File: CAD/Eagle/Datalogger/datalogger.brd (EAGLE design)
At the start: 48.2 x 50.5 mm, 12 parts

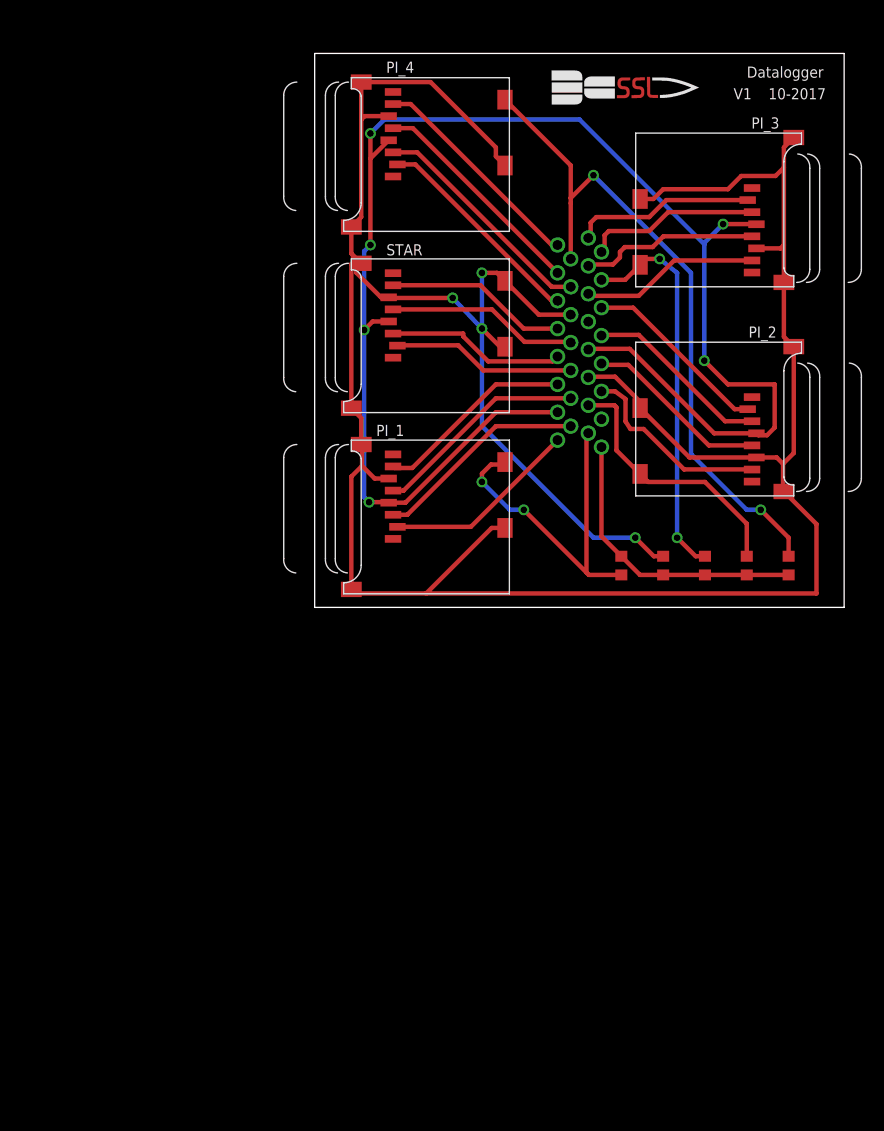
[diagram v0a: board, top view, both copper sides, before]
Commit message: Datalogger and STARduino
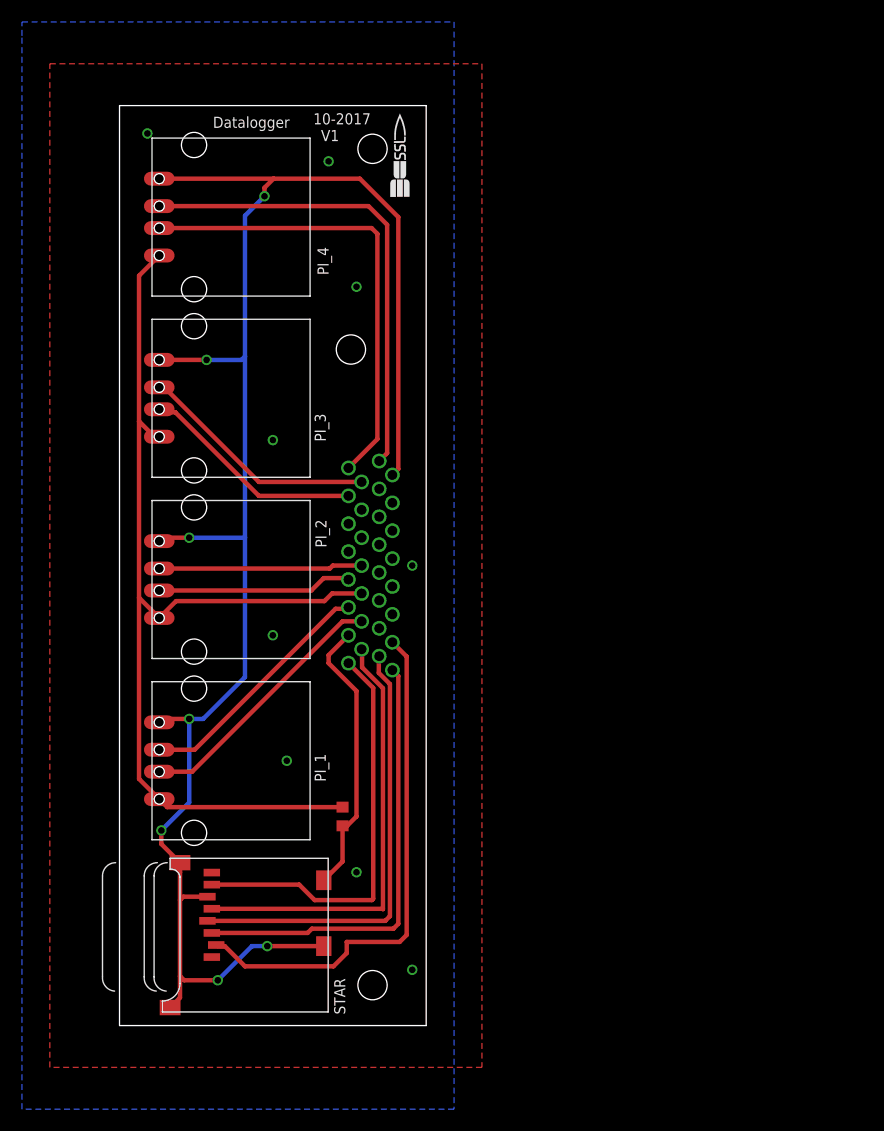
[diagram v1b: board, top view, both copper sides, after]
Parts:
- removed R1: 1M, resistor:R0603
- removed R2, R3, R4: (no value), resistor:R0603
- PI_1, PI_2, PI_3, PI_4: value MICROSD -> USB_A; device adafruit:MICROSD -> NR_connectors:USB_A
- U$1: value SSL.53IN -> SSL.3IN_SILK; device images:SSL_.53IN -> images:SSL_SILK_.3IN
- moved STAR 57.1 mm to (5.08, -22.9)
- moved PI_1 38.7 mm to (-3.81, -14.0)
- moved PI_3 38.2 mm to (-3.81, 19.1), turned to 270 degrees
- moved PI_2 37.6 mm to (-3.81, 2.54), turned to 270 degrees
- moved R5 37.1 mm to (6.35, -19.1), turned to 90 degrees
- moved PI_4 28.4 mm to (-3.81, 35.6)
- moved CONNECTOR 27.9 mm to (8.89, 3.81)
- moved U$1 19.3 mm to (10.4, 37.4), turned to 0 degrees
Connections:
- removed net CS_PI_1: CONNECTOR.17, PI_1.2
- removed net CS_PI_2: CONNECTOR.11, PI_2.2
- removed net CS_PI_3: CONNECTOR.16, PI_3.2
- removed net CS_PI_4: CONNECTOR.27, PI_4.2
- removed net MISO_PI_1: CONNECTOR.21, PI_1.7
- removed net MISO_PI_2: CONNECTOR.5, PI_2.7
- removed net MISO_PI_3: CONNECTOR.12, PI_3.7
- removed net MISO_PI_4: CONNECTOR.31, PI_4.7
- removed net MOSI_PI_1: CONNECTOR.18, PI_1.3
- removed net MOSI_PI_2: CONNECTOR.9, PI_2.3
- removed net MOSI_PI_3: CONNECTOR.15, PI_3.3
- removed net MOSI_PI_4: CONNECTOR.28, PI_4.3
- removed net SCK_PI_1: CONNECTOR.20, PI_1.5
- removed net SCK_PI_2: CONNECTOR.7, PI_2.5
- removed net SCK_PI_3: CONNECTOR.14, PI_3.5
- removed net SCK_PI_4: CONNECTOR.29, PI_4.5
- removed net SD_PI_1: CONNECTOR.2, PI_1.CD1, R1.1
- removed net SD_PI_2: CONNECTOR.4, PI_2.CD1, R2.1
- removed net SD_PI_3: CONNECTOR.13, PI_3.CD1, R3.1
- removed net SD_PI_4: CONNECTOR.30, PI_4.CD1, R4.1
- new net D: CONNECTOR.25
- new net DATA+1: CONNECTOR.21, PI_1.DATA+
- new net DATA+2: CONNECTOR.24, PI_2.DATA+
- new net DATA+3: CONNECTOR.30, PI_3.DATA+
- new net DATA+4: CONNECTOR.16, PI_4.DATA+
- new net DATA-1: CONNECTOR.20, PI_1.DATA-
- new net DATA-2: CONNECTOR.23, PI_2.DATA-
- new net DATA-3: CONNECTOR.29, PI_3.DATA-
- new net DATA-4: CONNECTOR.31, PI_4.DATA-
- new net FOUR: CONNECTOR.11
- new net N$7: CONNECTOR.12
- new net N$8: CONNECTOR.13
- new net ONE: CONNECTOR.27
- new net R: CONNECTOR.26
- new net THREE: CONNECTOR.10
- net +3V3: now also CONNECTOR.2; no longer CONNECTOR.19, CONNECTOR.8, PI_1.4, PI_2.4, PI_3.4, PI_4.4
- net +5V: now also CONNECTOR.22, PI_1.VCC, PI_2.VCC, PI_3.VCC, PI_4.VCC; no longer CONNECTOR.1, R1.2, R2.2, R3.2, R4.2
- net CS_STAR: now also CONNECTOR.3; no longer CONNECTOR.22
- net GND: now also CONNECTOR.15, PI_1.GND, PI_2.GND, PI_3.GND, PI_4.GND; no longer CONNECTOR.6, PI_1.6, PI_1.CD2, PI_1.MT1, PI_1.MT2, PI_2.6, PI_2.CD2, PI_2.MT1, PI_2.MT2, PI_3.6, PI_3.CD2, PI_3.MT1, PI_3.MT2, PI_4.6, PI_4.CD2, PI_4.MT1, PI_4.MT2
- net MISO_STAR: now also CONNECTOR.17; no longer CONNECTOR.25
- net MOSI_STAR: now also CONNECTOR.1; no longer CONNECTOR.23
- net SCK_STAR: now also CONNECTOR.18; no longer CONNECTOR.24
- net SD_STAR: now also CONNECTOR.19; no longer CONNECTOR.26
- net TWO: now also CONNECTOR.28; no longer CONNECTOR.3
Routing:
- net +3V3: track 143.2 -> 40.9 mm, vias 6 -> 0
- net +5V: track 26.6 -> 92.8 mm
- net SD_PI_4: track 62.7 -> 0.00 mm, vias 2 -> 0
- net GND: track 222.5 -> 165.0 mm, vias 2 -> 16
- net DATA+4: track 0.00 -> 43.3 mm
- net DATA-4: track 0.00 -> 42.5 mm
- net SD_PI_3: track 35.5 -> 0.00 mm, vias 2 -> 0
- net SD_PI_1: track 32.3 -> 0.00 mm, vias 2 -> 0
- net CS_STAR: track 16.7 -> 47.1 mm
- net MOSI_STAR: track 16.4 -> 40.7 mm
- net SD_PI_2: track 24.2 -> 0.00 mm
- net DATA-1: track 0.00 -> 24.1 mm
- net SCK_STAR: track 17.4 -> 40.1 mm
- net DATA+1: track 0.00 -> 22.6 mm
- net DATA+3: track 0.00 -> 22.0 mm
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- added copper zone on layer 1, net GND
- added copper zone on layer 16, net GND
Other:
- board size 48.2 x 50.5 mm -> 27.9 x 83.8 mm

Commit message: datalogger eagle and NX
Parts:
- removed PI_1, PI_2, PI_3, PI_4: USB_A, NR_connectors:USB_A
- removed R5: (no value), resistor:R0603
- removed STAR: MICROSD, adafruit:MICROSD
- added C1: 100nF, resistor:C0603
- added R1: 4.7k, resistor:R0603
- added R2: (no value), resistor:R0603
- added U$2, U$3: USB_A, NR_connectors:USB_A
- added U1: MT25QL01GBBB8ESF-0AAT, NR_IC:SOP2-16
- U$1: value SSL.3IN_SILK -> MICRO_SD; device images:SSL_SILK_.3IN -> NR_connectors:MICRO_SD_HINGED
- moved U$1 55.3 mm to (-8.51, -14.6), turned to 180 degrees
- moved CONNECTOR 15.3 mm to (10.2, 19.1)
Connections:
- removed net CS_STAR: CONNECTOR.3, STAR.2
- removed net D: CONNECTOR.25
- removed net FOUR: CONNECTOR.11
- removed net N$7: CONNECTOR.12
- removed net N$8: CONNECTOR.13
- removed net ONE: CONNECTOR.27
- removed net R: CONNECTOR.26
- removed net THREE: CONNECTOR.10
- removed net TWO: CONNECTOR.28
- new net MISO_FLASH: CONNECTOR.1, U1.8
- new net MOSI_FLASH: CONNECTOR.18, U1.15
- new net N$1: R1.2, U1.1, U1.3
- new net PB23: CONNECTOR.2, U1.7
- new net SCK_FLASH: CONNECTOR.17, U1.16
- net +3V3: now also C1.1, CONNECTOR.21, R1.1, U$1.VDD, U1.2; no longer CONNECTOR.2, STAR.4
- net +5V: now also CONNECTOR.29, R2.2, U$2.VCC1, U$2.VCC2, U$3.VCC1, U$3.VCC2; no longer CONNECTOR.22, PI_1.VCC, PI_2.VCC, PI_3.VCC, PI_4.VCC, R5.2
- net DATA+1: now also CONNECTOR.23, U$2.DATA+1; no longer CONNECTOR.21, PI_1.DATA+
- net DATA+2: now also CONNECTOR.25, U$2.DATA+2; no longer CONNECTOR.24, PI_2.DATA+
- net DATA+3: now also CONNECTOR.14, U$3.DATA+1; no longer CONNECTOR.30, PI_3.DATA+
- net DATA+4: now also U$3.DATA+2; no longer PI_4.DATA+
- net DATA-1: now also CONNECTOR.22, U$2.DATA-1; no longer CONNECTOR.20, PI_1.DATA-
- net DATA-2: now also CONNECTOR.26, U$2.DATA-2; no longer CONNECTOR.23, PI_2.DATA-
- net DATA-3: now also CONNECTOR.31, U$3.DATA-1; no longer CONNECTOR.29, PI_3.DATA-
- net DATA-4: now also CONNECTOR.30, U$3.DATA-2; no longer CONNECTOR.31, PI_4.DATA-
- net GND: now also C1.2, CONNECTOR.24, U$1.CD1, U$1.GND1, U$1.GND2, U$1.GND3, U$1.GND4, U$1.VSS, U$2.GND1, U$2.GND2, U$3.GND1, U$3.GND2, U1.10; no longer PI_1.GND, PI_2.GND, PI_3.GND, PI_4.GND, STAR.6, STAR.CD2, STAR.MT1, STAR.MT2
- net MISO_STAR: now also CONNECTOR.27, U$1.CMD; no longer CONNECTOR.17, STAR.7
- net MOSI_STAR: now also CONNECTOR.19, U$1.DAT0; no longer CONNECTOR.1, STAR.3
- net SCK_STAR: now also CONNECTOR.20, U$1.CLK; no longer CONNECTOR.18, STAR.5
- net SD_STAR: now also CONNECTOR.28, R2.1, U$1.CD; no longer CONNECTOR.19, R5.1, STAR.CD1
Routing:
- net CS_STAR: track 47.1 -> 0.00 mm
- net SD_STAR: track 25.6 -> 61.7 mm
- net DATA-4: track 42.5 -> 10.7 mm
- net DATA+4: track 43.3 -> 16.5 mm
- net PB23: track 0.00 -> 21.6 mm, vias 0 -> 2
- net MOSI_STAR: track 40.7 -> 20.8 mm
- net MISO_FLASH: track 0.00 -> 19.8 mm, vias 0 -> 2
- net +5V: track 92.8 -> 73.9 mm, vias 0 -> 3
- net DATA+1: track 22.6 -> 6.13 mm
- net DATA-1: track 24.1 -> 8.35 mm
- net SCK_STAR: track 40.1 -> 24.8 mm
- net SCK_FLASH: track 0.00 -> 15.1 mm
- net MOSI_FLASH: track 0.00 -> 14.8 mm
- net DATA-3: track 20.5 -> 6.13 mm
- net DATA+3: track 22.0 -> 11.1 mm
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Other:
- board size 27.9 x 83.8 mm -> 26.4 x 55.9 mm
- board text removed: "10-2017"
- board text removed: "Datalogger"
- board text removed: "V1"

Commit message: datalogger, mostly done
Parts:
- added U$4: SSL.3IN_SILK, images:SSL_SILK_.3IN
- moved U1 0.52 mm to (8.00, -5.71)
- moved U$1 0.34 mm to (-8.20, -14.7)
- moved R2 0.28 mm to (3.52, -13.4)
- moved R1 0.25 mm to (5.97, -13.5)
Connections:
- net DATA+1 renamed DATA1_P
- net DATA+2 renamed DATA2_P
- net DATA-1 renamed DATA1_N
- removed net DATA+3: CONNECTOR.14, U$3.DATA+1
- removed net DATA+4: CONNECTOR.16, U$3.DATA+2
- removed net DATA-2: CONNECTOR.26, U$2.DATA-2
- removed net DATA-3: CONNECTOR.31, U$3.DATA-1
- removed net DATA-4: CONNECTOR.30, U$3.DATA-2
- new net DATA2_N: CONNECTOR.24, U$2.DATA-2
- new net DATA3_N: CONNECTOR.30, U$3.DATA-1
- new net DATA3_P: CONNECTOR.31, U$3.DATA+1
- new net DATA4_N: CONNECTOR.16, U$3.DATA-2
- new net DATA4_P: CONNECTOR.15, U$3.DATA+2
- new net N$10: CONNECTOR.11
- new net N$11: CONNECTOR.12
- new net N$12: CONNECTOR.13
- new net N$2: CONNECTOR.3
- new net N$3: CONNECTOR.4
- new net N$4: CONNECTOR.5
- new net N$5: CONNECTOR.6
- new net N$6: CONNECTOR.7
- new net N$7: CONNECTOR.8
- new net N$8: CONNECTOR.9
- new net N$9: CONNECTOR.10
- net GND: now also CONNECTOR.14, CONNECTOR.26; no longer CONNECTOR.15, CONNECTOR.24
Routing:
- net DATA-2: track 26.1 -> 0.00 mm
- net DATA+4: track 16.5 -> 0.00 mm
- net DATA4_P: track 0.00 -> 16.2 mm
- net DATA4_N: track 0.00 -> 15.6 mm
- net DATA2_N: track 0.00 -> 13.2 mm
- net DATA+3: track 11.1 -> 0.00 mm
- net DATA-4: track 10.7 -> 0.00 mm
- net +5V: track 73.9 -> 63.4 mm, vias 3 -> 4
- net DATA3_N: track 0.00 -> 7.96 mm
- net DATA3_P: track 0.00 -> 7.83 mm
- net DATA2_P: track 19.1 -> 12.0 mm
- net DATA-3: track 6.13 -> 0.00 mm
- net MOSI_FLASH: track 14.8 -> 16.1 mm
- net DATA1_P: track 6.13 -> 7.28 mm
- net SCK_FLASH: track 15.1 -> 16.0 mm
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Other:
- board text added: "100nF"
- board text added: "11.2017"
- board text added: "1M"
- board text added: "4.7k"
- board text added: "B: Pi 2"
- board text added: "B: Pi 4"
- board text added: "Datalogger"
- board text added: "T: Pi 1"
- board text added: "T: Pi 3"
- board text added: "v.1"

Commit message: Datalogger v1 final
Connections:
- removed net N$11: CONNECTOR.12
- net DATA2_N: now also CONNECTOR.25; no longer CONNECTOR.24
- net DATA2_P: now also CONNECTOR.24; no longer CONNECTOR.25
- net GND: now also CONNECTOR.12
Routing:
- net GND: track 157.7 -> 117.4 mm, vias 19 -> 17
- net DATA2_P: track 12.0 -> 22.0 mm
- net DATA2_N: track 13.2 -> 22.0 mm
- net SD_STAR: track 62.0 -> 57.1 mm
- net DATA4_N: track 15.6 -> 19.2 mm
- net DATA4_P: track 16.2 -> 19.2 mm
- net SCK_FLASH: track 16.0 -> 13.2 mm
- net MISO_STAR: track 38.8 -> 36.3 mm
- net MOSI_FLASH: track 16.1 -> 14.4 mm
- net SCK_STAR: track 25.1 -> 23.5 mm
- net MOSI_STAR: track 21.2 -> 19.8 mm
- net +3V3: track 46.6 -> 45.5 mm
- net +5V: track 63.4 -> 63.0 mm, vias 4 -> 1
